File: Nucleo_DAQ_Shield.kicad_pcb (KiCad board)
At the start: 2 copper layers, 53.3 x 78.1 mm, 36 parts, among them J1 CONN_01X06, J2 CONN_01X06, J3 CONN_01X02, J4 CONN_01X02, J6 CONN_COAXIAL, J7 CONN_01X02, U1 4050, U10 ST_Nucleo144_F746ZG_CN10, U2 TL072, U3 L78L05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

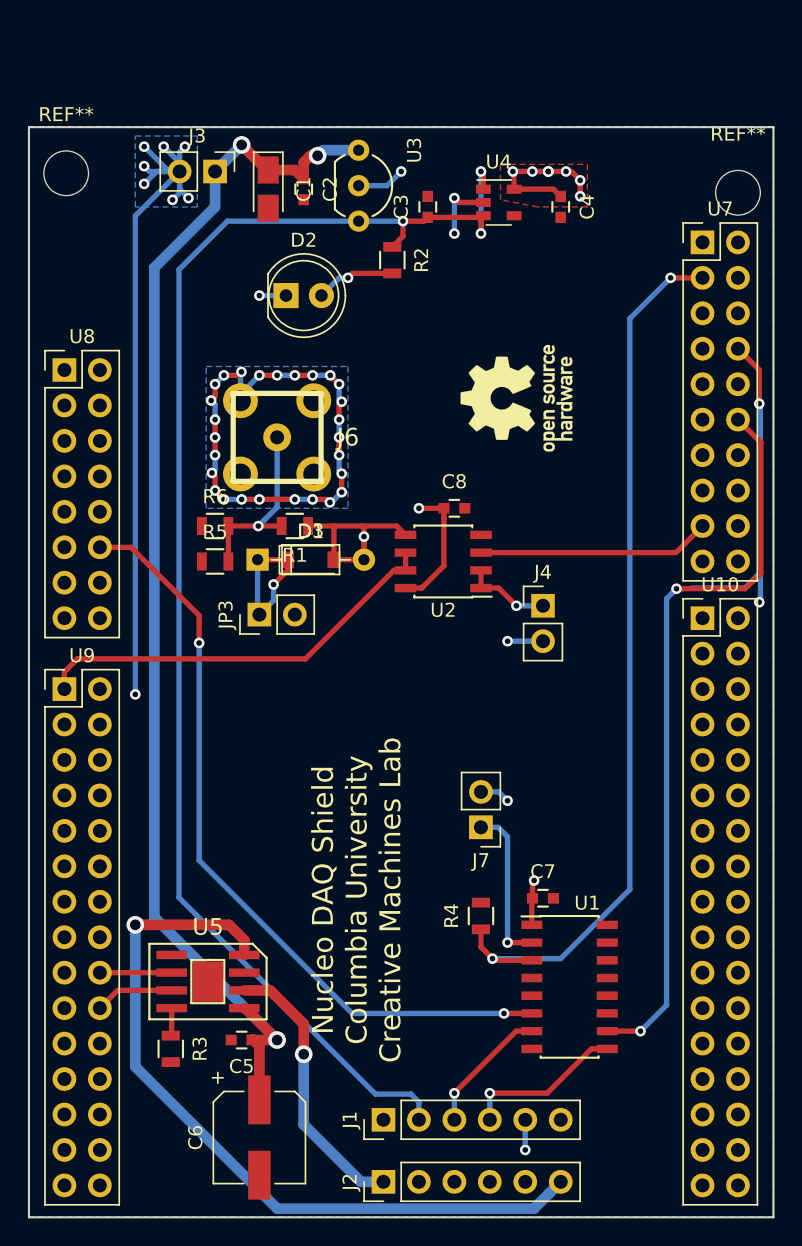
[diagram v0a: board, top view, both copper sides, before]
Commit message: Added silkscreen labels on Nucleo DAQ Shield PCB
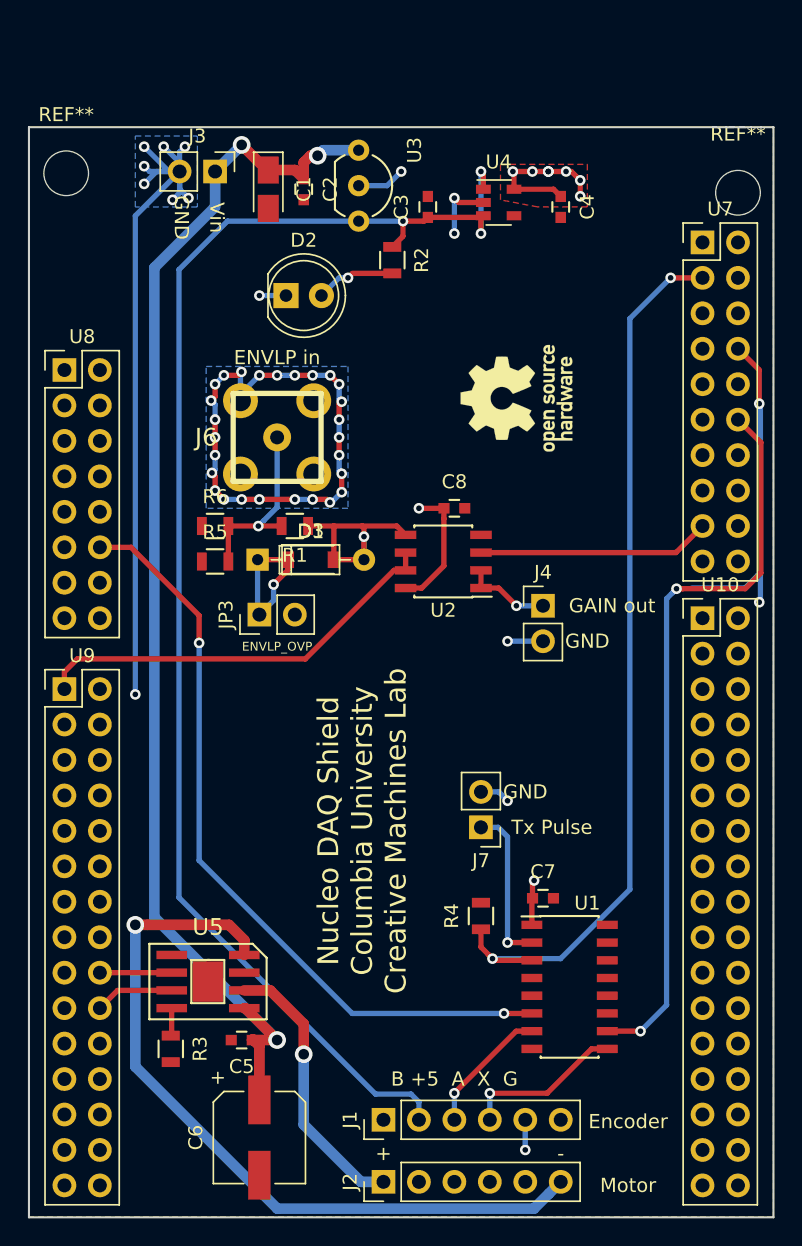
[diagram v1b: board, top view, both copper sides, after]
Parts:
- turned J6 to 270 degrees
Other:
- board text added: "+"
- board text added: "-"
- board text added: "B +5 A X G"
- board text added: "ENVLP in"
- board text added: "ENVLP_OVP"
- board text added: "Encoder"
- board text added: "GAIN out"
- board text added: "GND"
- board text added: "Motor"
- board text added: "Tx Pulse"
- board text added: "Vin"
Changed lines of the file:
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@@
     (links 80)
     (no_connects 0)
-    (area 133.708523 46.841 244.462898 129.674333)
+    (area 140.894999 48.819999 194.385001 127.075001)
     (thickness 1.6)
-    (drawings 22)
+    (drawings 35)
     (tracks 313)
     (zones 0)
@@
   )
   (module custom:SMA_uxcell (layer F.Cu)
-    (at 158.75 71.12 90)
+    (at 158.75 71.12 270)
     (tags "SMA Connector")
-    (fp_text reference J6 (at 0 5.08 180) (layer F.SilkS)
+    (fp_text reference J6 (at 0 5.08 360) (layer F.SilkS)
       (effects (font (thickness 0.3048)))
     )
-    (fp_text value CONN_COAXIAL (at 1.27 7.62 90) (layer F.SilkS) hide
+    (fp_text value CONN_COAXIAL (at 1.27 7.62 270) (layer F.SilkS) hide
       (effects (font (thickness 0.3048)))
     )
@@
     (fp_line (start 3.1496 3.1496) (end -3.1496 3.1496) (layer F.SilkS) (width 0.381))
     (fp_line (start -3.1496 3.1496) (end -3.1496 -3.1496) (layer F.SilkS) (width 0.381))
-    (pad 1 thru_hole circle (at 0 0 90) (size 1.99898 1.99898) (drill 1.00076) (layers *.Cu *.Mask F.SilkS)
+    (pad 1 thru_hole circle (at 0 0 270) (size 1.99898 1.99898) (drill 1.00076) (layers *.Cu *.Mask F.SilkS)
       (net 13 "Net-(J6-Pad1)"))
-    (pad 2 thru_hole circle (at 2.625 2.625 90) (size 2.5 2.5) (drill 1.5) (layers *.Cu *.Mask F.SilkS)
-      (net 2 GND))
-    (pad 2 thru_hole circle (at 2.625 -2.625 90) (size 2.5 2.5) (drill 1.5) (layers *.Cu *.Mask F.SilkS)
-      (net 2 GND))
-    (pad 2 thru_hole circle (at -2.625 2.625 90) (size 2.5 2.5) (drill 1.5) (layers *.Cu *.Mask F.SilkS)
-      (net 2 GND))
-    (pad 2 thru_hole circle (at -2.625 -2.625 90) (size 2.5 2.5) (drill 1.5) (layers *.Cu *.Mask F.SilkS)
+    (pad 2 thru_hole circle (at 2.625 2.625 270) (size 2.5 2.5) (drill 1.5) (layers *.Cu *.Mask F.SilkS)
+      (net 2 GND))
+    (pad 2 thru_hole circle (at 2.625 -2.625 270) (size 2.5 2.5) (drill 1.5) (layers *.Cu *.Mask F.SilkS)
+      (net 2 GND))
+    (pad 2 thru_hole circle (at -2.625 2.625 270) (size 2.5 2.5) (drill 1.5) (layers *.Cu *.Mask F.SilkS)
+      (net 2 GND))
+    (pad 2 thru_hole circle (at -2.625 -2.625 270) (size 2.5 2.5) (drill 1.5) (layers *.Cu *.Mask F.SilkS)
       (net 2 GND))
     (model connectors/sma.wrl
@@
     )
   )
-  (gr_text "Nucleo DAQ Shield\nColumbia University\nCreative Machines Lab" (at 164.465 104.267 90) (layer F.SilkS)
+  (gr_text - (at 179.07 122.428) (layer F.SilkS)
+    (effects (font (size 1.016 1.016) (thickness 0.1778)))
+  )
+  (gr_text + (at 166.37 122.428) (layer F.SilkS)
+    (effects (font (size 1.016 1.016) (thickness 0.1778)))
+  )
+  (gr_text "B +5  A  X  G" (at 171.45 117.094) (layer F.SilkS)
+    (effects (font (size 1.016 1.016) (thickness 0.1778)))
+  )
+  (gr_text Encoder (at 183.896 120.142) (layer F.SilkS)
+    (effects (font (size 1.016 1.016) (thickness 0.1778)))
+  )
+  (gr_text Motor (at 183.896 124.714) (layer F.SilkS)
+    (effects (font (size 1.016 1.016) (thickness 0.1778)))
+  )
+  (gr_text GND (at 151.892 55.372 270) (layer F.SilkS)
+    (effects (font (size 1.016 1.016) (thickness 0.1778)))
+  )
+  (gr_text Vin (at 154.432 55.372 270) (layer F.SilkS)
+    (effects (font (size 1.016 1.016) (thickness 0.1778)))
+  )
+  (gr_text ENVLP_OVP (at 158.75 86.106) (layer F.SilkS)
+    (effects (font (size 0.635 0.635) (thickness 0.127)))
+  )
+  (gr_text "ENVLP in" (at 158.75 65.405) (layer F.SilkS)
+    (effects (font (size 1.016 1.016) (thickness 0.1778)))
+  )
+  (gr_text GND (at 176.53 96.52) (layer F.SilkS)
+    (effects (font (size 1.016 1.016) (thickness 0.1778)))
+  )
+  (gr_text "Tx Pulse" (at 178.435 99.06) (layer F.SilkS)
+    (effects (font (size 1.016 1.016) (thickness 0.1778)))
+  )
+  (gr_text GND (at 180.975 85.725) (layer F.SilkS)
+    (effects (font (size 1.016 1.016) (thickness 0.1778)))
+  )
+  (gr_text "GAIN out" (at 182.753 83.185) (layer F.SilkS)
+    (effects (font (size 1.016 1.016) (thickness 0.1778)))
+  )
+  (gr_text "Nucleo DAQ Shield\nColumbia University\nCreative Machines Lab" (at 164.846 99.314 90) (layer F.SilkS)
     (effects (font (size 1.5 1.5) (thickness 0.3)))
   )

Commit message: Analog BOM & Nucleo pins added
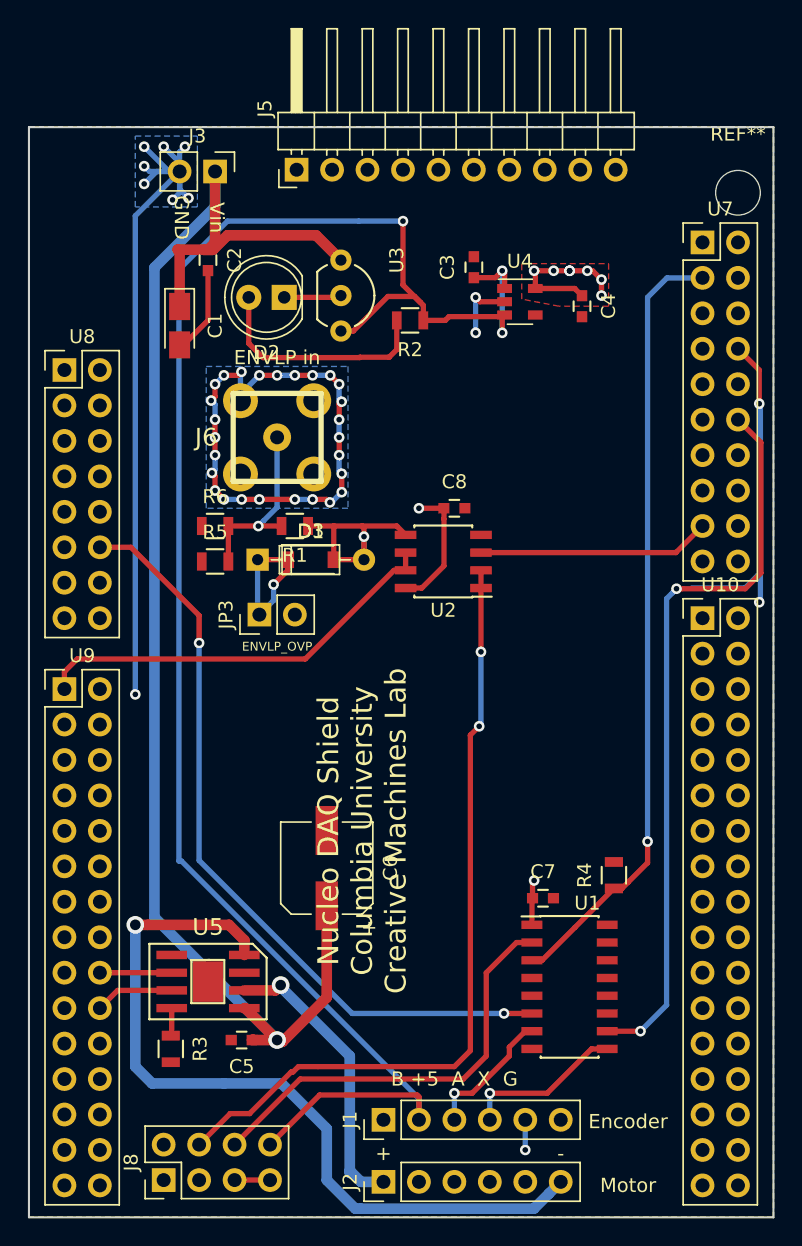
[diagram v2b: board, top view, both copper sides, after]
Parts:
- removed J4, J7: CONN_01X02, Pin_Headers:Pin_Header_Straight_1x02_Pitch2.54mm
- removed the REF** at (143.6, 52.2)
- removed REF***: OSHW-Logo_7.5x8mm_SilkScreen, Symbols:OSHW-Logo_7.5x8mm_SilkScreen
- added J5: CONN_01X10, Pin_Headers:Pin_Header_Angled_1x10_Pitch2.54mm, F.Cu at (160.1, 51.9)
- added J8: CONN_02X04, Pin_Headers:Pin_Header_Straight_2x04_Pitch2.54mm, F.Cu at (150.6, 124.3)
- U5: value DRV8881 -> DRV8871
- moved C6 19.9 mm to (162.3, 102.0), turned to 90 degrees
- moved C1 11.7 mm to (151.8, 63.1)
- moved R4 9.96 mm to (182.9, 102.5)
- moved C2 8.53 mm to (153.8, 58.4)
- moved U3 7.98 mm to (163.3, 58.4)
- moved C4 7.27 mm to (180.6, 61.7)
- moved U4 7.27 mm to (176.1, 61.4)
- moved C3 5.44 mm to (172.8, 58.9)
- moved R2 4.50 mm to (168.3, 62.7), turned to 180 degrees
- moved D2 0.18 mm to (159.3, 61.1), turned to 180 degrees
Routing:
- net /GAIN_buffered: track 6.24 -> 57.5 mm, vias 1 -> 2
- net +5V: track 102.2 -> 129.4 mm
- net /Tx_Pulse_buffered: track 11.5 -> 30.8 mm, vias 1 -> 0
- net Vbat: track 91.1 -> 107.2 mm, vias 3 -> 1
- net Net-(D2-Pad2): track 5.74 -> 16.7 mm, vias 1 -> 0
- net /Tx_Pulse: track 64.5 -> 56.2 mm, vias 2 -> 1
- net GND: track 135.8 -> 138.7 mm, vias 44 -> 40
- net /MOTOR-: track 55.0 -> 57.1 mm
- net /MOTOR+: track 19.9 -> 21.2 mm
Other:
- board text removed: "GAIN out"
- board text removed: "Tx Pulse"

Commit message: nucleo board updated
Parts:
- removed D3: SD103 DO-35, Diodes_THT:D_DO-35_SOD27_P7.62mm_Horizontal
- added J9: CONN_01X04, Pin_Headers:Pin_Header_Straight_1x04_Pitch2.54mm, F.Cu at (160.0, 116.8)
- J1: value CONN_01X06 -> CONN_01X05; footprint Pin_Headers:Pin_Header_Straight_1x06_Pitch2.54mm -> Pin_Headers:Pin_Header_Straight_1x05_Pitch2.54mm
- moved J1 10.2 mm to (176.5, 120.3), turned to 270 degrees
- moved C5 9.53 mm to (156.1, 104.8)
- moved U5 9.40 mm to (153.7, 100.7)
- moved R3 9.15 mm to (151.4, 105.8)
- moved J8 7.55 mm to (151.5, 116.8), turned to 0 degrees
- moved C6 2.95 mm to (165.2, 101.6)
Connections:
- J1 pad 1: Net-(J1-Pad1) -> GND
- J1 pad 2: +5V -> /5V_CUI_X
- J1 pad 4: /5V_CUI_X -> +5V
- J1 pad 5: GND -> Net-(J1-Pad5)
- J8 pad 6: /Tx_Pulse_buffered -> +5V
- J8 pad 8: +5V -> /Tx_Pulse_buffered
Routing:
- net /MOTOR+: track 21.2 -> 30.4 mm
- net /MOTOR-: track 57.1 -> 48.4 mm
- net /MOTOR_PWM_FORWARD: track 5.67 -> 14.1 mm
- net /MOTOR_PWM_REVERSE: track 5.51 -> 13.4 mm
- net /GAIN_buffered: track 57.5 -> 50.3 mm
- net /ENCODER_A: track 55.1 -> 48.7 mm
- net 20V: track 0.00 -> 5.97 mm
- net GND: track 138.7 -> 143.5 mm
- net +5V: track 129.4 -> 134.1 mm
- net /Tx_Pulse_buffered: track 30.8 -> 34.7 mm
- net /ENVLP: track 16.0 -> 14.4 mm, vias 1 -> 0
- net (no net): track 0.00 -> 1.65 mm, vias 0 -> 1
- net Vbat: track 107.2 -> 105.7 mm
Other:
- board text added: "--GND--"
- board text added: "-20V-"
- board text added: "-5V-"
- board text added: "Gain"
- board text added: "Tx"

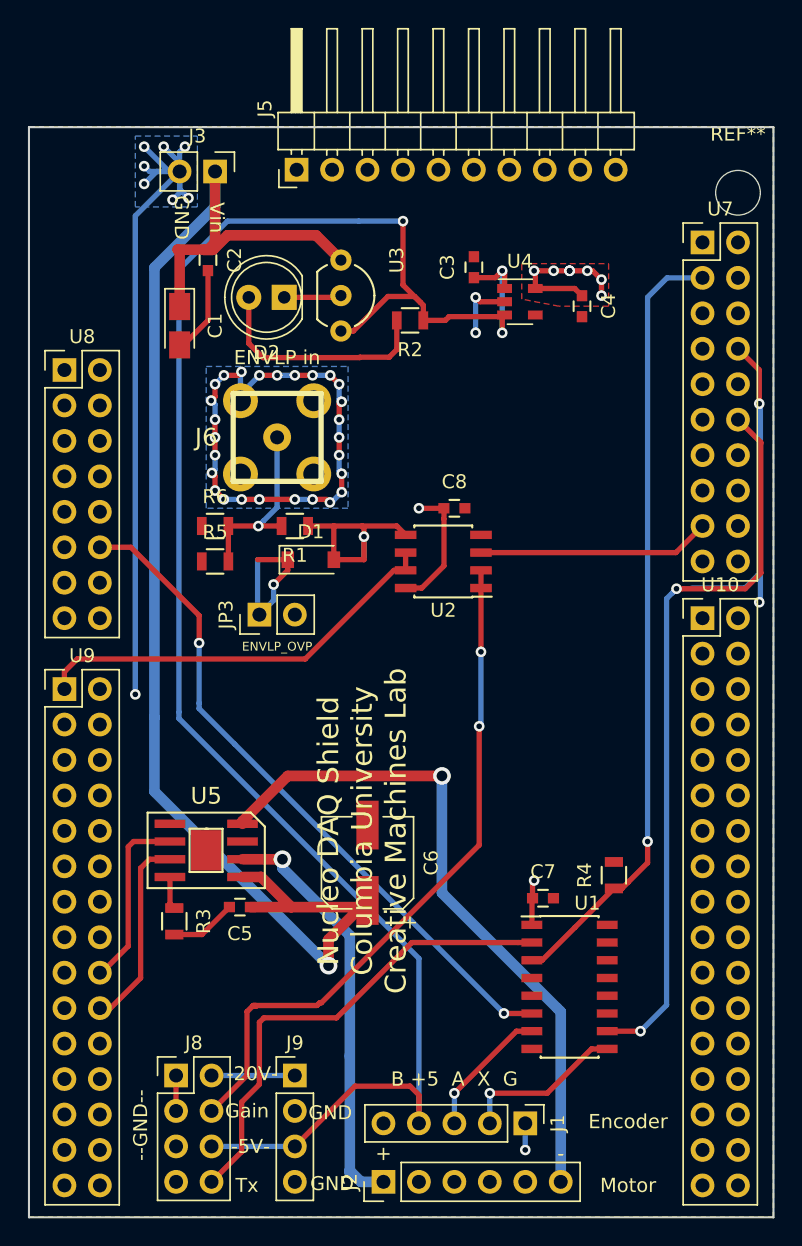
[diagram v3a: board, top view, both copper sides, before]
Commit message: Updated IMU connector and encoder pins
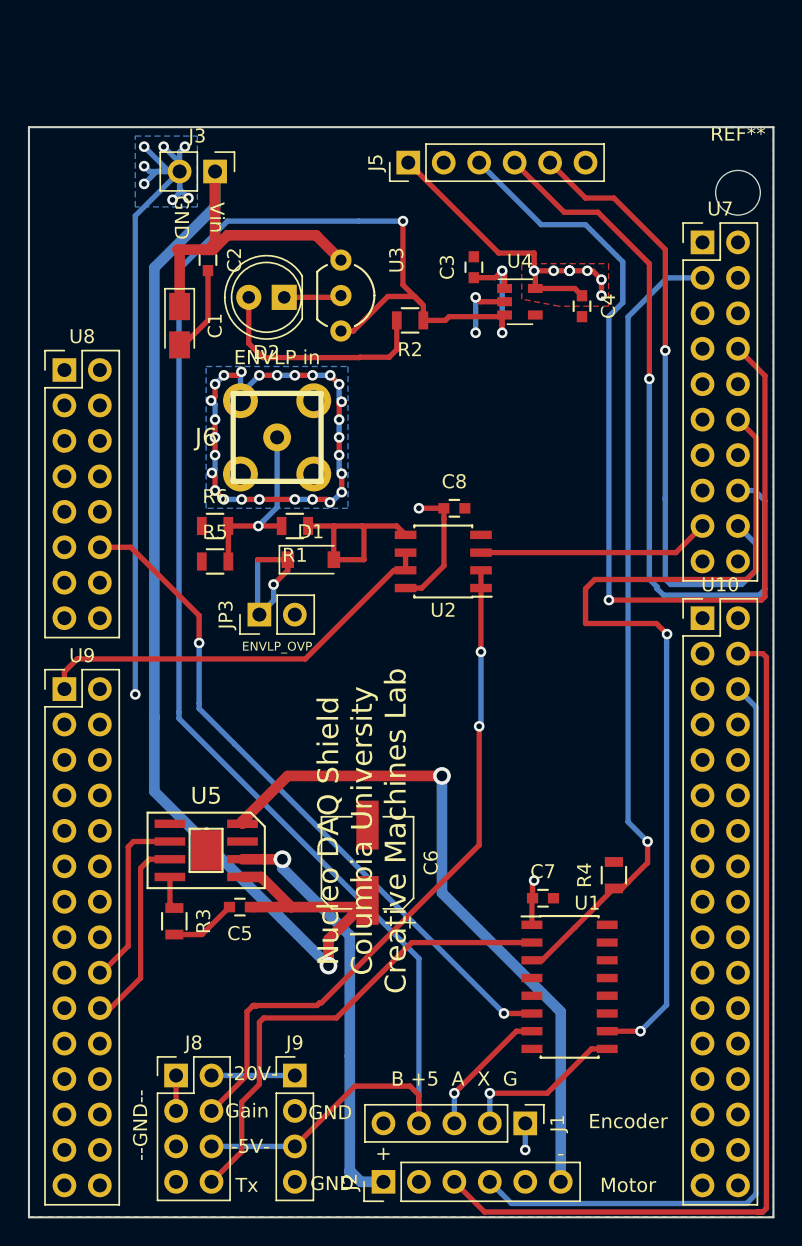
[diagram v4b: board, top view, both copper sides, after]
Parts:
- J5: value CONN_01X10 -> CONN_01X06; footprint Pin_Headers:Pin_Header_Angled_1x10_Pitch2.54mm -> Pin_Headers:Pin_Header_Straight_1x06_Pitch2.54mm
- moved J5 8.02 mm to (168.1, 51.4)
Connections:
- J2 pad 3: Net-(J2-Pad3) -> /ENCODERA
- J2 pad 4: Net-(J2-Pad4) -> /ENCODERB
- J5 pad 1: Net-(J5-Pad1) -> +3.3VA
- J5 pad 3: Net-(J5-Pad3) -> GND
- J5 pad 4: Net-(J5-Pad4) -> /SDA
- J5 pad 5: Net-(J5-Pad5) -> /SCL
- U10 pad 4: Net-(U10-Pad4) -> /ENCODERA
- U10 pad 6: Net-(U10-Pad6) -> /ENCODERB
- U7 pad 16: Net-(U7-Pad16) -> /SDA
- U7 pad 18: Net-(U7-Pad18) -> /SCL
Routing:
- net /ENCODERA: track 0.00 -> 65.4 mm
- net /ENCODERB: track 0.00 -> 56.7 mm
- net /SDA: track 0.00 -> 53.4 mm, vias 0 -> 1
- net /SCL: track 0.00 -> 45.5 mm, vias 0 -> 1
- net GND: track 143.5 -> 187.1 mm, vias 40 -> 39
- net +3.3VA: track 23.7 -> 36.7 mm
- net /ENCODER_X: track 53.3 -> 64.4 mm
- net (no net): track 1.65 -> 0.00 mm, vias 1 -> 0
- net /Tx_Pulse: track 56.2 -> 57.4 mm
